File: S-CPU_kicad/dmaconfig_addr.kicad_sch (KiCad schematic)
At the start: 112 parts

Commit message: Fix ERC errors in schematics.
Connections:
- net DMA_BANK1_DOUT0: now also OLGV0.1 (IN), OLGV0.3 (IN)
- net DMA_BANK1_DOUT1: now also OLGV1.1 (IN), OLGV1.3 (IN)
- net DMA_BANK1_DOUT2: now also OLGV2.1 (IN), OLGV2.3 (IN)
- net DMA_BANK1_DOUT3: now also OLGV3.1 (IN), OLGV3.3 (IN)
- net DMA_BANK1_DOUT4: now also OLCO0.1 (IN), OLCO0.3 (IN)
- net DMA_BANK1_DOUT5: now also OLCO1.1 (IN), OLCO1.3 (IN)
- net DMA_BANK1_DOUT6: now also OLCO2.1 (IN), OLCO2.3 (IN)
- net DMA_BANK1_DOUT7: now also OLCO3.1 (IN), OLCO3.3 (IN)
- net CYCLE_COUNTER0 renamed PATTERN_COUNTER0
- net CYCLE_COUNTER1 renamed PATTERN_COUNTER1
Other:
- title: SNES S-CPU Schematics  -> Reverse Engineered SNES S-CPU Schematics 
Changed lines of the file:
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@@
   (paper "A1")
   (title_block
-    (title "SNES S-CPU Schematics ")
+    (title "Reverse Engineered SNES S-CPU Schematics ")
     (date "2023-10-21")
     (rev "0.1")
@@
     (effects (font (size 1.27 1.27)) (justify left bottom))
   )
+  (label "DMA_BANK1_DOUT5" (at 626.11 340.36 0) (fields_autoplaced)
+    (effects (font (size 1.27 1.27)) (justify left bottom))
+  )
   (label "DMA_A3" (at 590.55 179.07 180) (fields_autoplaced)
     (effects (font (size 1.27 1.27)) (justify right bottom))
@@
     (effects (font (size 1.27 1.27)) (justify left bottom))
   )
+  (label "DMA_BANK1_DOUT6" (at 626.11 356.87 0) (fields_autoplaced)
+    (effects (font (size 1.27 1.27)) (justify left bottom))
+  )
   (label "DMA_A14" (at 781.05 125.73 180) (fields_autoplaced)
     (effects (font (size 1.27 1.27)) (justify right bottom))
@@
     (effects (font (size 1.27 1.27)) (justify left bottom))
   )
+  (label "DMA_BANK1_DOUT4" (at 626.11 330.2 0) (fields_autoplaced)
+    (effects (font (size 1.27 1.27)) (justify left bottom))
+  )
   (label "DMA_BANK2_DOUT6" (at 721.36 130.81 0) (fields_autoplaced)
     (effects (font (size 1.27 1.27)) (justify left bottom))
@@
     (effects (font (size 1.27 1.27)) (justify left bottom))
   )
-  (label "~{MODE5}" (at 362.585 48.26 0) (fields_autoplaced)
-    (effects (font (size 1.27 1.27)) (justify left bottom))
-  )
   (label "DMA_BANK1_DOUT2" (at 626.11 201.93 0) (fields_autoplaced)
     (effects (font (size 1.27 1.27)) (justify left bottom))
@@
     (effects (font (size 1.27 1.27)) (justify right bottom))
   )
-  (label "CYCLE_COUNTER1" (at 238.76 273.05 0) (fields_autoplaced)
+  (label "PATTERN_COUNTER1" (at 238.76 273.05 0) (fields_autoplaced)
     (effects (font (size 1.27 1.27)) (justify left bottom))
   )
@@
     (effects (font (size 1.27 1.27)) (justify right bottom))
   )
-  (label "~{DMA_BANK1_RD}" (at 605.79 256.54 0) (fields_autoplaced)
+  (label "DMA_BANK1_DOUT0" (at 626.11 276.86 0) (fields_autoplaced)
     (effects (font (size 1.27 1.27)) (justify left bottom))
   )
@@
     (effects (font (size 1.27 1.27)) (justify right bottom))
   )
-  (label "CYCLE_COUNTER0" (at 238.76 267.97 0) (fields_autoplaced)
+  (label "PATTERN_COUNTER0" (at 238.76 267.97 0) (fields_autoplaced)
     (effects (font (size 1.27 1.27)) (justify left bottom))
   )
@@
     (effects (font (size 1.27 1.27)) (justify left bottom))
   )
+  (label "DMA_BANK1_DOUT1" (at 626.11 287.02 0) (fields_autoplaced)
+    (effects (font (size 1.27 1.27)) (justify left bottom))
+  )
   (label "DMA_BANK0_DOUT7" (at 530.86 367.03 0) (fields_autoplaced)
     (effects (font (size 1.27 1.27)) (justify left bottom))
@@
     (effects (font (size 1.27 1.27)) (justify left bottom))
   )
+  (label "DMA_BANK1_DOUT3" (at 626.11 313.69 0) (fields_autoplaced)
+    (effects (font (size 1.27 1.27)) (justify left bottom))
+  )
   (label "DMA_BANK2_DOUT7" (at 721.36 367.03 0) (fields_autoplaced)
     (effects (font (size 1.27 1.27)) (justify left bottom))
@@
     (effects (font (size 1.27 1.27)) (justify right bottom))
   )
-  (label "~{DMA_BANK2_RD}" (at 701.04 256.54 0) (fields_autoplaced)
-    (effects (font (size 1.27 1.27)) (justify left bottom))
-  )
   (label "DMA_BANK2_DOUT5" (at 721.36 340.36 0) (fields_autoplaced)
     (effects (font (size 1.27 1.27)) (justify left bottom))
@@
     (effects (font (size 1.27 1.27)) (justify left bottom))
   )
-  (label "~{DMA_BANK0_RD}" (at 509.27 256.54 0) (fields_autoplaced)
-    (effects (font (size 1.27 1.27)) (justify left bottom))
-  )
   (label "D3" (at 687.07 313.69 180) (fields_autoplaced)
     (effects (font (size 1.27 1.27)) (justify right bottom))
@@
     (effects (font (size 1.27 1.27)) (justify right bottom))
   )
+  (label "DMA_BANK1_DOUT7" (at 626.11 367.03 0) (fields_autoplaced)
+    (effects (font (size 1.27 1.27)) (justify left bottom))
+  )
   (label "DMA_BANK2_DOUT2" (at 721.36 201.93 0) (fields_autoplaced)
     (effects (font (size 1.27 1.27)) (justify left bottom))
   )
+  (label "DMA_BANK1_DOUT2" (at 626.11 303.53 0) (fields_autoplaced)
+    (effects (font (size 1.27 1.27)) (justify left bottom))
+  )
   (label "DMA_BANK0_DOUT3" (at 530.86 313.69 0) (fields_autoplaced)
     (effects (font (size 1.27 1.27)) (justify left bottom))
@@
     (effects (font (size 1.27 1.27)) (justify left))
   )
-  (hierarchical_label "CYCLE_COUNTER[0..1]" (shape input) (at 226.06 275.59 180) (fields_autoplaced)
+  (hierarchical_label "PATTERN_COUNTER[0..1]" (shape input) (at 226.06 275.59 180) (fields_autoplaced)
+    (effects (font (size 1.27 1.27)) (justify right))
+  )
+  (hierarchical_label "~{DMA_BANK0_RD}" (shape input) (at 509.27 256.54 180) (fields_autoplaced)
     (effects (font (size 1.27 1.27)) (justify right))
   )
@@
     (effects (font (size 1.27 1.27)) (justify right))
   )
+  (hierarchical_label "~{DMA_BANK2_RD}" (shape input) (at 701.04 256.54 180) (fields_autoplaced)
+    (effects (font (size 1.27 1.27)) (justify right))
+  )
+  (hierarchical_label "~{MODE5}" (shape input) (at 362.585 48.26 180) (fields_autoplaced)
+    (effects (font (size 1.27 1.27)) (justify right))
+  )
+  (hierarchical_label "~{DMA_BANK1_RD}" (shape input) (at 605.79 256.54 180) (fields_autoplaced)
+    (effects (font (size 1.27 1.27)) (justify right))
+  )

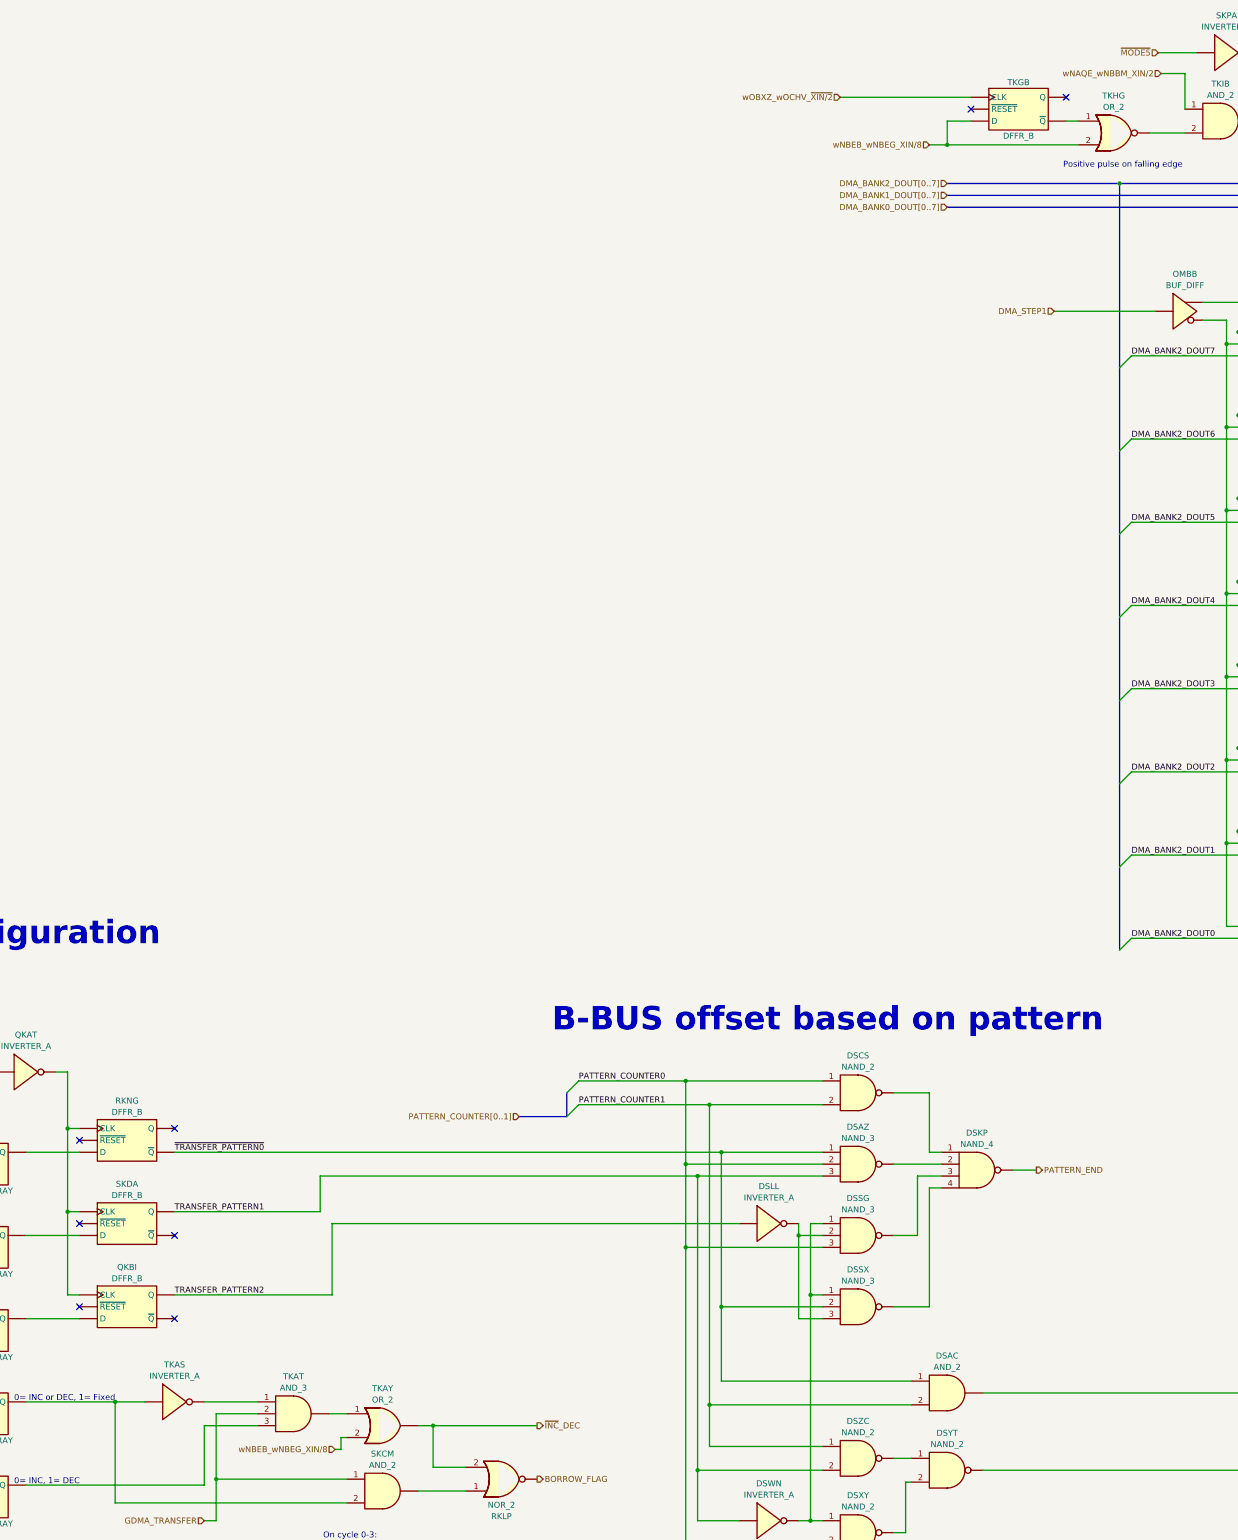
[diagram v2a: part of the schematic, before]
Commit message: Big rework on the hierachical sheet to make thigs a bit clearer. PDF exported for Rev 0.1.
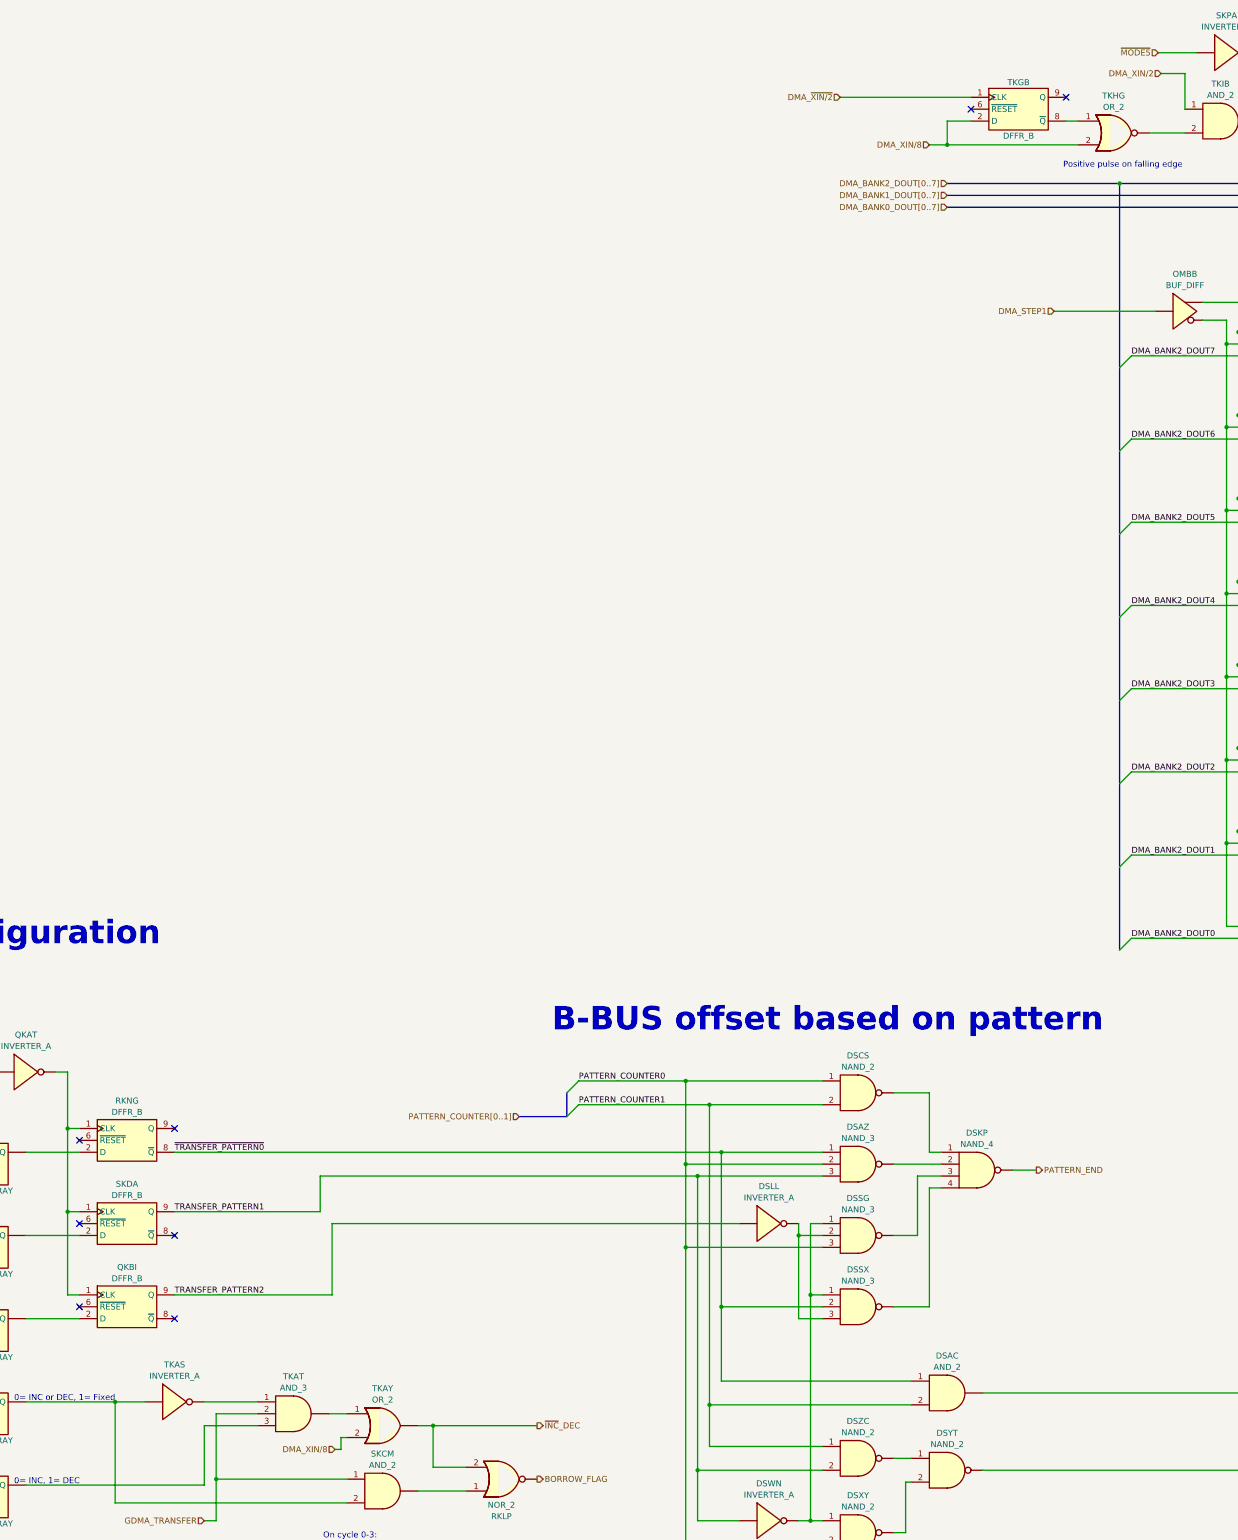
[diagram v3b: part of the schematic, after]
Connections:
- net TRANSFER_PATTERN1: now also SKDA.9 (Q); no longer SKDA.7 (Q)
- net TRANSFER_PATTERN2: now also QKBI.9 (Q); no longer QKBI.7 (Q)
- net ~{TRANSFER_PATTERN0}: now also RKNG.8 (~{Q}); no longer RKNG.6 (~{Q})
- net DMA_~{XIN/2}: now reaches TKGB.1 (CLK)
- net DMA_~{XIN/2}: no longer TKGB.5 (~{RESET})
- net at TKGB.6 (~{RESET}): no longer TKHG.1
- net at RKNG.1 (CLK): now also QKAT.2, QKBI.1 (CLK), SKDA.1 (CLK); no longer RKNG.5 (~{RESET})
- net wNAQE_wNBBM_XIN/2 renamed DMA_XIN/2
- net wNBEB_wNBEG_XIN/8 renamed DMA_XIN/8
- removed net wOBXZ_wOCHV_~{XIN/2}: TKGB.3 (CLK), TKGB.4 (~{CLK})
- new net: TKGB.8 (~{Q}), TKHG.1

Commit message: Fixed VAWR which should have been an SR DFF (to fix issue #3 raised in github)
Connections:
- net at OMDK0.1 (~{ENA}), OMDK1.1 (~{ENA}), OMDK2.1 (~{ENA})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: now also OMBB.3; no longer OMBB.2
- net at PKBB0.1 (~{ENA}), PKBB1.1 (~{ENA}), PKBB2.1 (~{ENA})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: now also PKBG.3; no longer PKBG.2
- net at QKAG0.1 (~{ENA}), QKAG1.1 (~{ENA}), QKAG2.1 (~{ENA})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: now also QKAI.3; no longer QKAI.2
- net at SKKP0.1 (~{ENA}), SKKP1.1 (~{ENA}), SKKP2.1 (~{ENA})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: now also SKJF.3; no longer SKJF.2
- net at PKEM0.1 (~{ENA}), PKEM1.1 (~{ENA}), PKEM2.1 (~{ENA})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: now also PKEJ.3; no longer PKEJ.2
- net at OLCL0.1 (~{ENA}), OLCL1.1 (~{ENA}), OLCL2.1 (~{ENA})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: now also OKWN.3; no longer OKWN.2
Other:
- moved on the sheet: DSYT, DSZC, OKWN, OLCL0, OLCL1, OLCL2, OLCL3, OLCL4, OLCL5, OLCL6, OLCL7, OLMD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
